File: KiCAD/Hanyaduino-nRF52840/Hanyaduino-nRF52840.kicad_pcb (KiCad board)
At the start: 2 copper layers, 34.7 x 17.8 mm, 37 parts, among them J1 Conn_01x02_Male, J2 Arduino_pro_micro_conn, J3 USB_B_Micro, J4 Conn_01x04_Male, Q1 DMG3415U, U1 MCP73831-2-OT, U2 NRF52832_MODULE_MDBT42, U3 CP2104, U4 AP2113(3.3V), Y1 32.768KHz

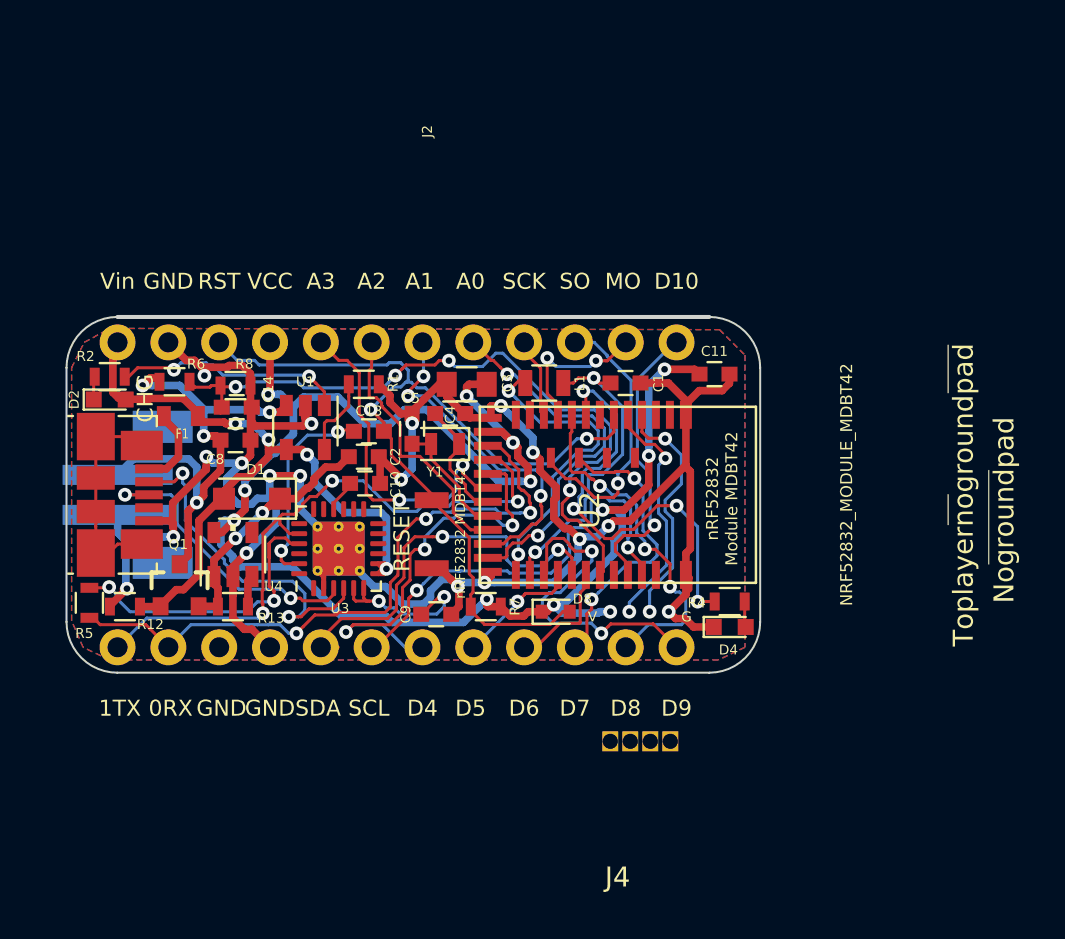
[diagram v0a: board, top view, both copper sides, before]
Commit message: Add neopixel and delete crystal
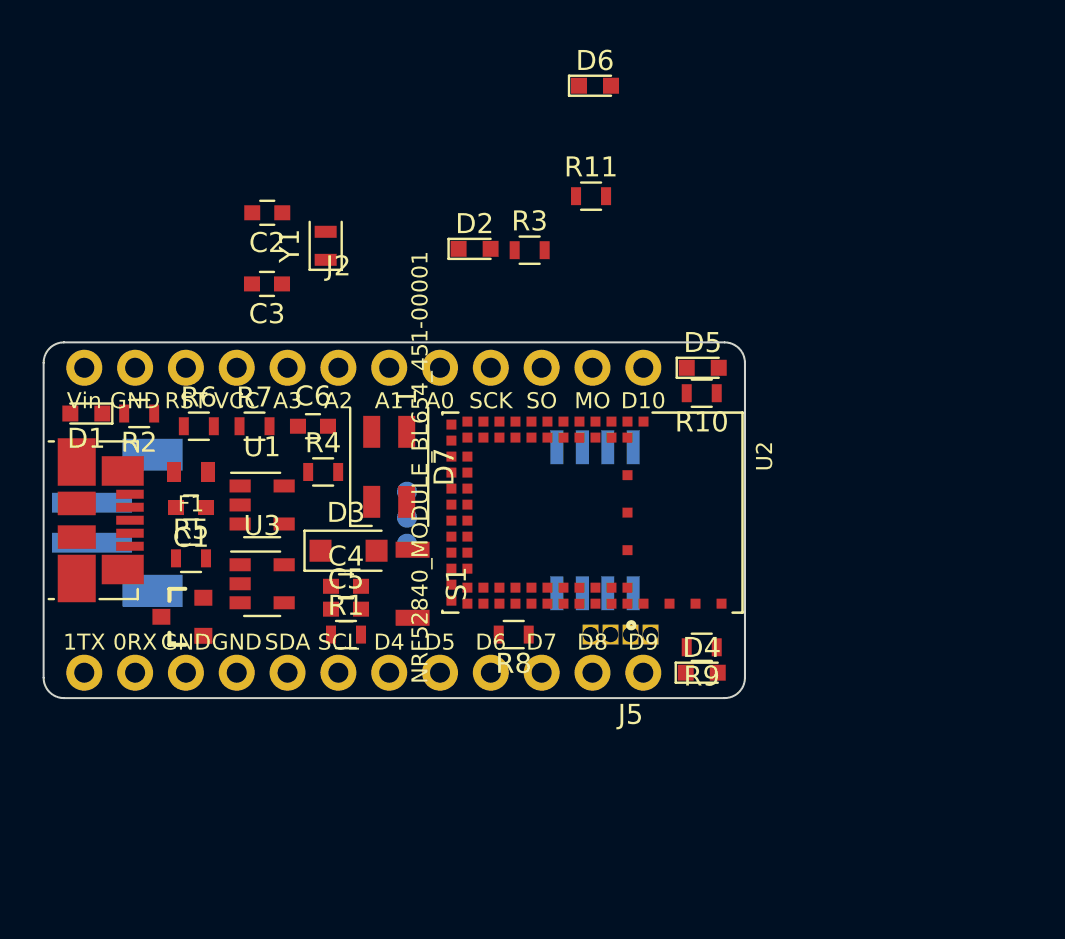
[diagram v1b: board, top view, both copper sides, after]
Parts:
- removed C10: 10uf, Capacitors_SMD:C_0603
- removed C11, C8: 10uF, Capacitors_SMD:C_0603
- removed C13, C9: 0.1uF, Capacitors_SMD:C_0603
- removed C14: 1nF, Capacitors_SMD:C_0603
- removed D8: 1N4148, Diodes_SMD:D_SOD-523
- removed L1: 10uH, Inductors_SMD:L_0805
- removed R12: 100K, Resistors_SMD:R_0603
- removed R13: 10K, Resistors_SMD:R_0603
- removed RESET: RST SW, library:B3U-1000P(OMRON Ultra-small Tactile Switch)
- added C6: 1nF, Capacitors_SMD:C_0603, F.Cu at (125.7, 112.1)
- added D3: MBR120, Diodes_SMD:D_SOD-123F, F.Cu at (127.5, 118.4)
- added D5: USR LED2, LEDs:LED_0603, F.Cu at (145.2, 109.2)
- added D6: PWR LED, LEDs:LED_0603, F.Cu at (139.8, 95.1)
- added D7: SK6812, KiCAD footprints:LED_SK6812MINI_PLCC4_3.5x3.5mm_P1.75mm, F.Cu at (129.5, 114.2)
- added J5: Conn_01x04_Male, library:Conn4 1.0mm pitch, F.Cu at (141.6, 122.6)
- added R10: 1K, Resistors_SMD:R_0603, F.Cu at (145.2, 110.5)
- added R11: 220R, Resistors_SMD:R_0603, F.Cu at (139.6, 100.6)
- added R3: 1K, Resistors_SMD:R_0603, F.Cu at (136.6, 103.3)
- added R9: 1K, Resistors_SMD:R_0603, F.Cu at (145.2, 123.2)
- added S1: RST SW, library:B3U-1000P(OMRON Ultra-small Tactile Switch), F.Cu at (130.8, 120.0)
- C1: value 1uF -> 10uF
- C2: value 10uF -> 22pF
- C3: value 10uF -> 22pF; footprint Capacitors_SMD:C_0805 -> Capacitors_SMD:C_0603
- C4, C5: value 22pF -> 10uF
- D1: value MBR120 -> CHG; footprint Diodes_SMD:D_SOD-123F -> LEDs:LED_0603
- D2: value CHG -> DONE
- J1: value Conn_01x02_Male -> Conn_01x02_Female; footprint Connectors_JST:JST_PH_B2B-PH-SM4-TB_02x2.00mm_Straight -> library:3 point pad
- J3: value USB_B_Micro -> Conn_01x02_Male; footprint library:USB_Micro-B_Molex_47346-0001 -> Connectors_JST:JST_PH_B2B-PH-SM4-TB_02x2.00mm_Straight; moved to B.Cu
- J4: value Conn_01x04_Male -> USB_B_Micro; footprint library:Conn4 1.0mm pitch -> library:USB_Micro-B_Molex_47346-0001
- R4: value 1K -> 100K
- R5: value 1K -> 10K
- R7: value 10K -> 2M
- R8: value 2M -> 10k
- U2: value NRF52832_MODULE_MDBT42 -> NRF52840_MODULE_BL654_451-00001; footprint library:MDBT42 -> BL654-nRF52840-451-00001:XCVR_451-00001
- U3: value CP2104 -> AP2113(3.3V); footprint KiCAD footprints:QFN-24-1EP_4x4mm_P0.5mm_EP2.7x2.6mm_ThermalVias -> KiCAD footprints:SOT-23-5
- U4: value AP2113(3.3V) -> W25Q32; footprint KiCAD footprints:SOT-23-5 -> Housings_SOIC:SOIJ-8_5.3x5.3mm_Pitch1.27mm; moved to B.Cu
- moved J4 28.6 mm to (115.3, 116.8)
- moved C1 22.6 mm to (119.6, 116.2), turned to 180 degrees
- moved R4 21.3 mm to (126.2, 114.4), turned to 0 degrees
- moved D2 19.7 mm to (133.8, 103.3)
- moved R8 18.7 mm to (135.8, 122.6), turned to 180 degrees
- moved U4 18.2 mm to (139.8, 116.8)
- moved R7 14.7 mm to (122.8, 112.1)
- moved J1 13.4 mm to (130.4, 116.7)
- moved C2 13.1 mm to (123.4, 101.5), turned to 180 degrees
- moved R1 12.5 mm to (127.4, 122.6), turned to 0 degrees
- moved Y1 11.6 mm to (126.4, 103.1), turned to 90 degrees
- moved C3 11.2 mm to (123.4, 105.0)
- moved C4 10.1 mm to (127.4, 120.1)
- moved C5 9.60 mm to (127.4, 121.3), turned to 0 degrees
- moved D1 9.31 mm to (114.4, 111.5)
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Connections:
- net /P0.10/NFC2 renamed D32/data3(QSPI)
- net /SWO renamed Net-(U2-Pad7)
- net Net-(U2-Pad2) renamed D36
- C1 pad 1: Net-(C1-Pad1) -> VBAT
- C2 pad 1: Net-(C2-Pad1) -> XL1
- C3 pad 1: VCC -> XL2
- C5 pad 1: Net-(C5-Pad1) -> VCC
- D1 pad 1: Net-(C2-Pad1) -> Net-(D1-Pad1)
- D2 pad 1: Net-(D2-Pad1) -> GND
- D2 pad 2: VBUS -> Net-(D2-Pad2)
- J1 pad 1: GND -> D12/RX
- J1 pad 2: VBAT -> D11/TX
- J2 pad 1: TX -> D0/TX
- J2 pad 10: D7 -> D7(button)
- J2 pad 11: D12 -> D8/NeoPixel
- J2 pad 13: D10/SS -> D10
- J2 pad 14: MOSI -> D25/MOSI(SPI)
- J2 pad 15: MISO -> D24/MISO(SPI)
- J2 pad 16: SCK -> D26/SCK(SPI)
- J2 pad 17: A0 -> D14/A0
- J2 pad 18: A1 -> D15/A1
- J2 pad 19: A2 -> D16/A2
- J2 pad 2: RX -> D1/RX
- J2 pad 20: A3 -> D17/A3
- J2 pad 5: SDA -> D22/SDA(I2C)
- J2 pad 6: SCL -> D23/SCL(I2C)
- J2 pad 7: D11 -> D4/LED2
- J2 pad 9: D6/A7 -> D6
- J3 pad 1: Net-(F1-Pad1) -> GND
- J3 pad 2: D- -> VBAT
- J4 pad 1: VCC -> Net-(F1-Pad1)
- J4 pad 2: SWDIO -> D-
- J4 pad 3: SWCLK -> D+
- J4 pad 4: GND -> Net-(J4-Pad4)
- Q1 pad 2: Net-(C2-Pad1) -> Net-(C4-Pad1)
- R2 pad 2: Net-(D2-Pad1) -> Net-(D1-Pad1)
- R4 pad 1: Net-(D4-Pad2) -> GND
- R4 pad 2: /LED1 -> VBUS
- R5 pad 2: RX -> Net-(C4-Pad1)
- R6 pad 2: A5 -> D20/A6(Battery)
- R7 pad 1: RESET -> D20/A6(Battery)
- R7 pad 2: VCC -> GND
- R8 pad 1: A5 -> D28/CS(QSPI)
- R8 pad 2: GND -> VCC
- U2 pad 1: GND -> SWDIO
- U2 pad 10: MOSI -> D1/RX
- U2 pad 11: SCK -> D30/data1(QSPI)
- U2 pad 13: /P0.09/NFC1 -> D28/CS(QSPI)
- U2 pad 14: GND -> D27/CLK(QSPI)
- U2 pad 15: VCC -> D+
- U2 pad 16: RX -> D29/data0(QSPI)
- U2 pad 17: TX -> D-
- U2 pad 18: D11 -> D24/MISO(SPI)
- U2 pad 19: A3 -> RESET
- U2 pad 20: Net-(C4-Pad1) -> D25/MOSI(SPI)
- U2 pad 21: Net-(C5-Pad1) -> D8/NeoPixel
- U2 pad 22: A2 -> D26/SCK(SPI)
- U2 pad 23: A1 -> GND
- U2 pad 24: A0 -> VBUS
- U2 pad 25: GND -> VCC
- U2 pad 26: Net-(L1-Pad2) -> GND
- U2 pad 27: Net-(C1-Pad1) -> D23/SCL(I2C)
- U2 pad 28: D9 -> D22/SDA(I2C)
- U2 pad 29: D5 -> D12/RX
- U2 pad 3: /FRST -> SWCLK
- U2 pad 30: SDA -> D13
- U2 pad 31: D6/A7 -> VCC
- U2 pad 32: A5 -> D5
- U2 pad 33: A4 -> GND
- U2 pad 34: D10/SS -> D14/A0
- U2 pad 35: SCL -> D11/TX
- U2 pad 36: /LED2 -> D9
- U2 pad 37: GND -> D6
- U2 pad 38: Net-(U2-Pad38) -> D10
- U2 pad 39: DFU -> D15/A1
- U2 pad 4: SWCLK -> D7(button)
- U2 pad 40: D7 -> GND
- U2 pad 41: MISO -> XL2
- U2 pad 5: SWDIO -> D35
- U2 pad 6: RESET -> D33
- U2 pad 8: /LED1 -> D0/TX
- U2 pad 9: D12 -> D31/data2(QSPI)
- U3 pad 1: Net-(U3-Pad1) -> Net-(C4-Pad1)
- U3 pad 3: D+ -> Net-(R5-Pad1)
- U3 pad 4: D- -> Net-(U3-Pad4)
- U3 pad 5: VCCIO -> VCC
- U4 pad 1: Net-(C2-Pad1) -> D28/CS(QSPI)
- U4 pad 2: GND -> D29/data0(QSPI)
- U4 pad 3: Net-(R13-Pad1) -> VCC
- U4 pad 4: Net-(U4-Pad4) -> GND
- U4 pad 5: VCC -> D30/data1(QSPI)
- Y1 pad 1: Net-(C4-Pad1) -> XL2
- Y1 pad 2: Net-(C5-Pad1) -> XL1
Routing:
- net GND: track 127.7 -> 0.00 mm, vias 18 -> 0
- net VCC: track 78.0 -> 0.00 mm, vias 12 -> 0
- net RESET: track 44.7 -> 0.00 mm, vias 2 -> 0
- net VBUS: track 36.1 -> 0.00 mm, vias 4 -> 0
- net A5: track 35.5 -> 0.00 mm, vias 4 -> 0
- net RX: track 32.4 -> 0.00 mm, vias 3 -> 0
- net TX: track 31.5 -> 0.00 mm, vias 3 -> 0
- net VBAT: track 28.2 -> 0.00 mm, vias 4 -> 0
- net SCL: track 21.9 -> 0.00 mm, vias 2 -> 0
- net /LED1: track 21.9 -> 0.00 mm, vias 4 -> 0
- net D11: track 21.5 -> 0.00 mm, vias 3 -> 0
- net SDA: track 20.1 -> 0.00 mm, vias 2 -> 0
- net A0: track 18.6 -> 0.00 mm, vias 2 -> 0
- net D12: track 18.4 -> 0.00 mm, vias 3 -> 0
- net A3: track 17.6 -> 0.00 mm, vias 2 -> 0
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- removed copper zone on B.Cu, net GND
- removed copper zone on F.Cu, net GND
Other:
- board size 34.7 x 17.8 mm -> 35.1 x 17.8 mm
- board text removed: "."
- board text removed: "CHG"
- board text removed: "D12"
- board text removed: "D13"
- board text removed: "D14"
- board text removed: "D2"
- board text removed: "D25"
- board text removed: "D26"
- board text removed: "D3"
- board text removed: "D4"
- board text removed: "D5"
- board text removed: "D6"
- board text removed: "D8"
- board text removed: "G"
- board text removed: "GND"
- board text removed: "Hanyaduino nRF52 v0.81 Nov 10, 2018"
- board text removed: "SWCLK"
- board text removed: "SWDIO"
- board text removed: "V"
- board text removed: "VCC"
- board text removed: "nRF52832 MDBT42"
- board text removed: "nRF52832 Module MDBT42"

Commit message: layout
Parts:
- removed C2, C3: 22pF, Capacitors_SMD:C_0603
- removed D2: DONE, LEDs:LED_0603
- removed D6: PWR LED, LEDs:LED_0603
- removed J5: Conn_01x04_Male, library:Conn4 1.0mm pitch
- removed R11: 220R, Resistors_SMD:R_0603
- removed R3: 1K, Resistors_SMD:R_0603
- removed Y1: 32.768KHz, Crystals:Crystal_SMD_TXC_9HT11-2pin_2.0x1.2mm
- J1: value Conn_01x02_Female -> Conn_01x03_Female
- moved J1 5.48 mm to (126.4, 113.0), turned to 0 degrees
- moved C1 3.27 mm to (118.9, 119.4)
- moved C4 2.33 mm to (125.3, 119.2)
- moved R8 2.05 mm to (137.8, 122.3)
- moved S1 1.64 mm to (129.4, 119.3)
- moved D3 1.50 mm to (126.1, 117.9)
- moved U1 1.30 mm to (123.4, 114.8), turned to 180 degrees
- moved R4 1.28 mm to (126.4, 113.2), turned to 180 degrees
- moved C6 1.20 mm to (124.6, 111.8), turned to 180 degrees
- moved U3 1.17 mm to (123.2, 121.2)
- moved R1 1.09 mm to (126.7, 121.7), turned to 180 degrees
- moved C5 1.07 mm to (126.7, 120.4)
- moved D7 0.92 mm to (129.0, 113.4)
- moved R7 0.78 mm to (122.0, 112.0), turned to 90 degrees
- moved R6 0.64 mm to (119.5, 112.5)
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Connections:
- J1 pad 3: (no net) -> GND
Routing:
- net GND: track 0.00 -> 161.5 mm, vias 0 -> 23
- net VCC: track 0.00 -> 66.3 mm, vias 0 -> 10
- net VBUS: track 0.00 -> 47.6 mm, vias 0 -> 6
- net D0/TX: track 0.00 -> 36.2 mm, vias 0 -> 3
- net D1/RX: track 0.00 -> 32.5 mm, vias 0 -> 3
- net D+: track 0.00 -> 29.0 mm, vias 0 -> 2
- net D4/LED2: track 0.00 -> 28.8 mm, vias 0 -> 2
- net D-: track 0.00 -> 26.7 mm, vias 0 -> 2
- net VBAT: track 0.00 -> 25.4 mm, vias 0 -> 4
- net RESET: track 0.00 -> 22.9 mm, vias 0 -> 3
- net D8/NeoPixel: track 0.00 -> 21.6 mm, vias 0 -> 3
- net Net-(C4-Pad1): track 0.00 -> 20.7 mm, vias 0 -> 5
- net D3/LED1: track 0.00 -> 19.5 mm, vias 0 -> 4
- net D6: track 0.00 -> 18.0 mm, vias 0 -> 3
- net D9: track 0.00 -> 17.7 mm, vias 0 -> 3
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- added copper zone on B.Cu, net GND
- added copper zone on F.Cu, net GND

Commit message: v0.81
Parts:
- removed S1: RST SW, library:B3U-1000P(OMRON Ultra-small Tactile Switch)
- removed U4: W25Q32, Housings_SOIC:SOIJ-8_5.3x5.3mm_Pitch1.27mm
- added RESET: RST SW, library:B3U-1000P(OMRON Ultra-small Tactile Switch), F.Cu at (129.4, 119.3)
- added SPI flash: W25Q32, Housings_SOIC:SOIJ-8_5.3x5.3mm_Pitch1.27mm, B.Cu at (139.8, 116.8)
- U2: value NRF52840_MODULE_BL654_451-00001 -> BL654(nRF52840)
- renumbered J3 to Li-Po, J2 to e
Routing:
- net GND: track 161.5 -> 164.4 mm
- net D17/A3: track 11.3 -> 13.5 mm
- net D20/A6(Battery): track 17.5 -> 19.4 mm
- net D27/CLK(QSPI): track 8.58 -> 10.1 mm
- net D6: track 18.0 -> 16.7 mm
- net D26/SCK(SPI): track 13.6 -> 14.7 mm
- net D16/A2: track 10.2 -> 9.14 mm
- net D3/LED1: track 19.5 -> 20.5 mm
- net D29/data0(QSPI): track 13.7 -> 14.4 mm
- net D24/MISO(SPI): track 17.2 -> 17.8 mm
- net D10: track 12.6 -> 13.2 mm
- net D7(button): track 13.4 -> 13.9 mm
- net VCC: track 66.3 -> 66.8 mm
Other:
- board text added: "CHG"
- board text added: "G"
- board text added: "GND"
- board text added: "Hanyaduino nRF52840 Rev 0.81 Dec 11, 2018"
- board text added: "Happy birthday!"
- board text added: "RX"
- board text added: "TX"
- board text added: "V"

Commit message: Hanyaduino-nRF52840 v1.0
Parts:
- removed e: Arduino_pro_micro_conn, library:Arduino_pro_micro_conn
- added J2: Arduino_pro_micro_conn, library:Arduino_pro_micro_conn, F.Cu at (126.9, 114.3)
- added REF**: OSHW-Logo2_7.3x6mm_SilkScreen, KiCAD footprints:OSHW-Logo2_7.3x6mm_SilkScreen, B.Cu at (124.6, 119.5)
- D7: value SK6812 -> SK6812MINI
- U2: value BL654(nRF52840) -> NRF52840 BL654
- moved J1 1.58 mm to (124.9, 112.4)
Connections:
- D7 pad 1: VCC -> Net-(D7-Pad1)
- D7 pad 2: Net-(D7-Pad2) -> GND
- D7 pad 3: GND -> D8/NeoPixel
- D7 pad 4: D8/NeoPixel -> VCC
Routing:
- net D18/A4: track 0.00 -> 21.6 mm, vias 0 -> 3
- net D4/LED2: track 28.7 -> 10.00 mm
- net D19/A5: track 0.00 -> 16.9 mm, vias 0 -> 4
- net GND: track 164.4 -> 149.7 mm, vias 23 -> 24
- net D8/NeoPixel: track 21.6 -> 10.0 mm, vias 3 -> 2
- net RESET: track 23.4 -> 30.1 mm
- net D+: track 29.0 -> 26.2 mm
- net D12/RX: track 10.5 -> 12.8 mm
- net D-: track 26.7 -> 24.6 mm
- net D6: track 16.7 -> 14.6 mm
- net D28/CS(QSPI): track 11.8 -> 13.5 mm
- net D22/SDA(I2C): track 15.2 -> 16.9 mm
- net D3/LED1: track 20.5 -> 18.9 mm
- net D10: track 13.2 -> 14.8 mm
- net D26/SCK(SPI): track 14.7 -> 13.3 mm
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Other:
- board text added: "+"
- board text added: "-"
- board text added: "Hanyaduino nRF52840 Rev 1.0 Dec 16, 2018"
- board text removed: "Hanyaduino nRF52840 Rev 0.81 Dec 11, 2018"
- board text removed: "Happy birthday!"

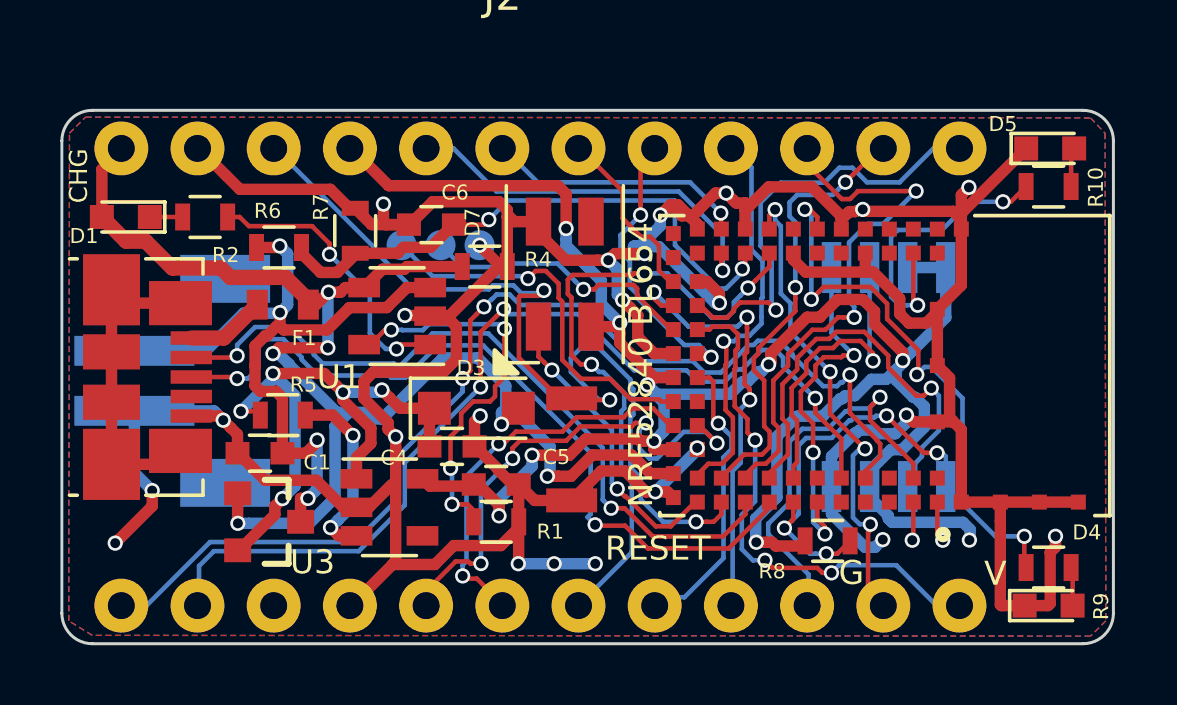
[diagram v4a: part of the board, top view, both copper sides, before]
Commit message: Hanyaduino nRF52840 v1.01 (Add JST SH battery connector)
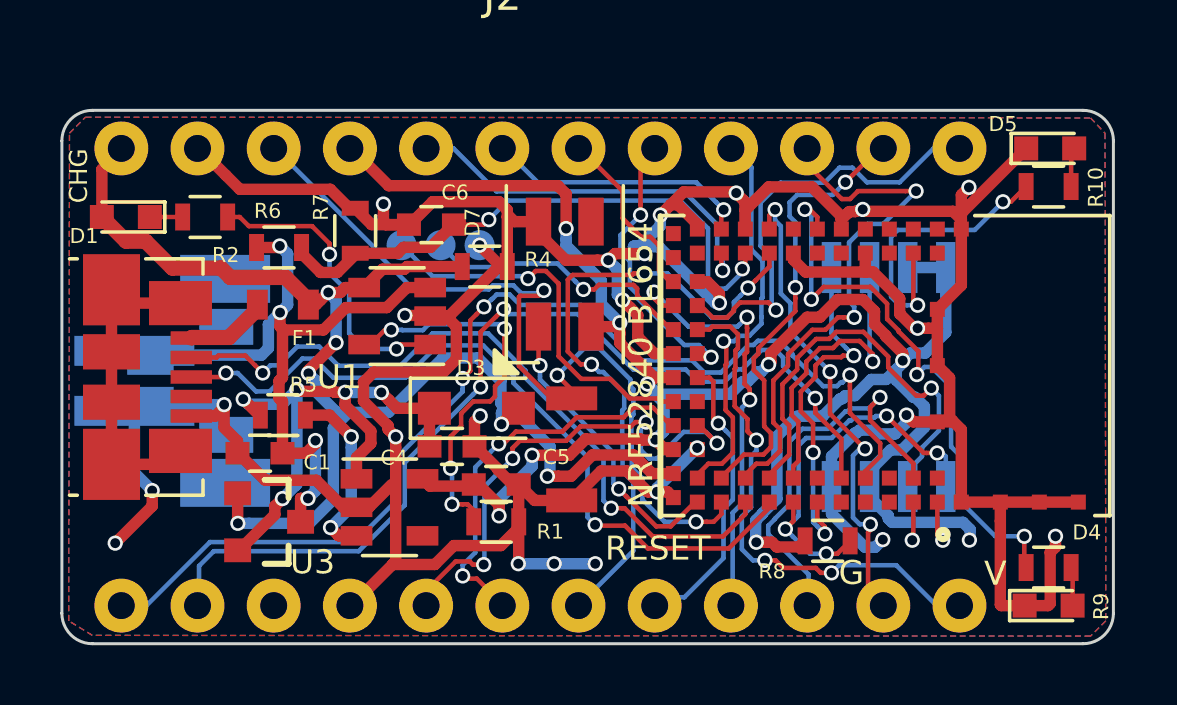
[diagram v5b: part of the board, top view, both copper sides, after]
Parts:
- added Li-Po: Conn_01x02_Male, library:JST_SH_BM02B-SRSS-TB_02x1.00mm_Straight, B.Cu at (116.5, 117.0)
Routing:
- net RESET: track 30.1 -> 27.9 mm
- net VBUS: track 48.0 -> 45.9 mm
- net Net-(C4-Pad1): track 20.5 -> 19.3 mm
- net D+: track 26.2 -> 25.6 mm
- net VBAT: track 24.8 -> 24.2 mm
- net GND: track 149.7 -> 150.0 mm, vias 24 -> 25
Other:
- board text added: "Hanyaduino nRF52840 Rev 1.01 Jan 3, 2019"
- board text removed: "Hanyaduino nRF52840 Rev 1.0 Dec 16, 2018"

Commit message: Hanyaduino nRF52840 v1.5
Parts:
- removed SPI flash: W25Q32, Housings_SOIC:SOIJ-8_5.3x5.3mm_Pitch1.27mm
- added U4: W25Q32, Housings_SOIC:SOIJ-8_5.3x5.3mm_Pitch1.27mm, B.Cu at (139.8, 116.8)
- U2: value NRF52840 BL654 -> nRF52840 BL654
- moved Li-Po 0.28 mm to (116.8, 117.0)
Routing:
- net D32/data3(QSPI): track 0.00 -> 8.94 mm, vias 0 -> 1
- net VCC: track 67.5 -> 58.8 mm, vias 10 -> 9
- net D29/data0(QSPI): track 14.4 -> 8.16 mm
- net GND: track 150.0 -> 155.0 mm, vias 25 -> 26
- net D31/data2(QSPI): track 0.00 -> 3.47 mm, vias 0 -> 1
- net RESET: track 27.9 -> 24.6 mm
- net VBAT: track 24.2 -> 26.4 mm
- net D30/data1(QSPI): track 12.3 -> 10.3 mm, vias 3 -> 1
- net D19/A5: track 16.9 -> 18.7 mm
- net D27/CLK(QSPI): track 10.3 -> 8.65 mm
- net D4/LED2: track 10.00 -> 8.53 mm
- net D26/SCK(SPI): track 13.3 -> 14.4 mm
- net D9: track 17.5 -> 18.6 mm
- net D28/CS(QSPI): track 13.5 -> 14.5 mm
- net D18/A4: track 21.6 -> 22.5 mm
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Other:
- board text added: "Hanyaduino nRF52840 Rev 1.5 Jan 5, 2019"
- board text removed: "Hanyaduino nRF52840 Rev 1.01 Jan 3, 2019"
